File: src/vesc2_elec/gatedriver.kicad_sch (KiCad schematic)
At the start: 1 part, among them U101 DRV8301

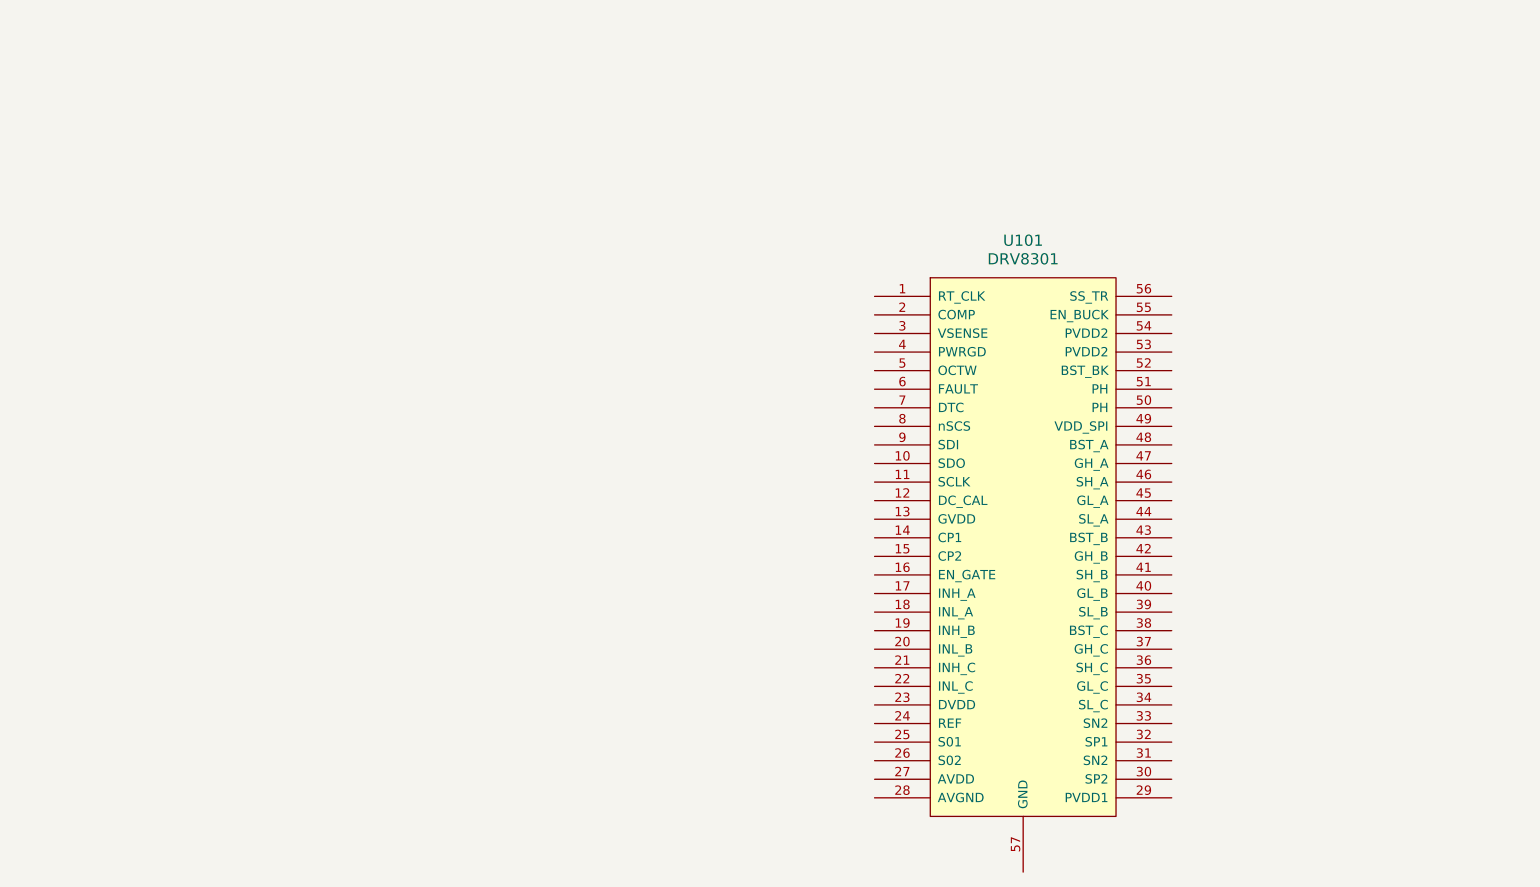
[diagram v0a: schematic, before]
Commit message: recreate gate driver looking less ugly
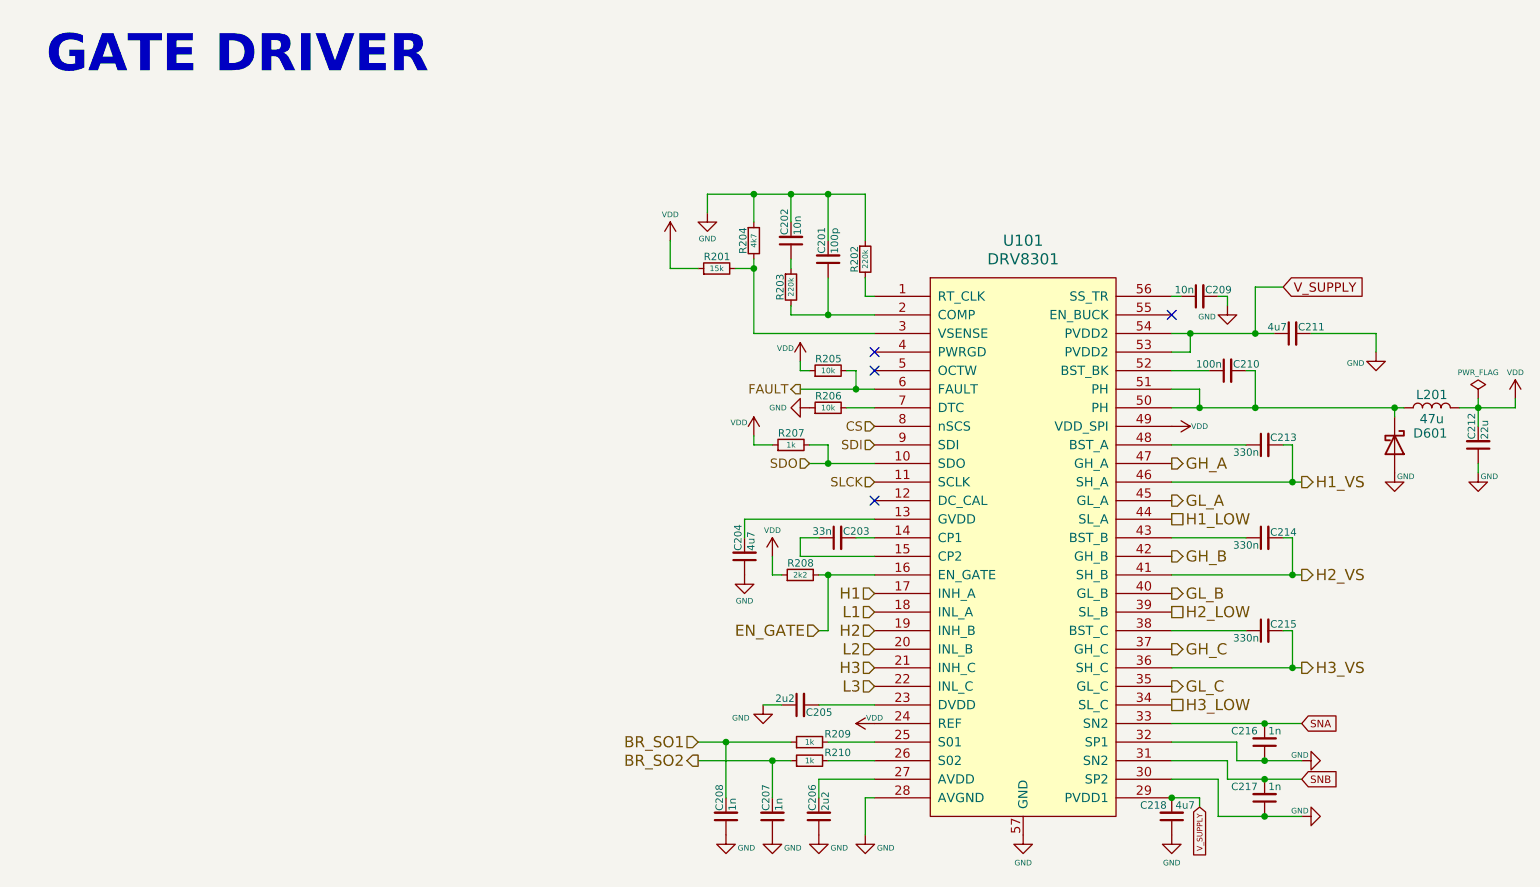
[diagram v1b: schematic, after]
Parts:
- added C201: 100p, Capacitor_SMD:C_0402_1005Metric, symbol Bluesat:C_CompactV
- added C202: 10n, Capacitor_SMD:C_0402_1005Metric, symbol Bluesat:C_CompactV
- added C203: 33n, Capacitor_SMD:C_0603_1608Metric, symbol Bluesat:C_CompactH
- added C204: 4u7, Capacitor_SMD:C_1206_3216Metric, symbol Bluesat:C_CompactV
- added C205: 2u2, Capacitor_SMD:C_0603_1608Metric, symbol Bluesat:C_CompactH
- added C206: 2u2, Capacitor_SMD:C_0603_1608Metric, symbol Bluesat:C_CompactV
- added C207, C208, C216, C217: 1n, Capacitor_SMD:C_0402_1005Metric, symbol Bluesat:C_CompactV
- added C209: 10n, Capacitor_SMD:C_0402_1005Metric, symbol Bluesat:C_CompactH
- added C210: 100n, Capacitor_SMD:C_0603_1608Metric, symbol Bluesat:C_CompactH
- added C211: 4u7, Capacitor_SMD:C_1210_3225Metric, symbol Bluesat:C_CompactH
- added C212: 22u, Capacitor_SMD:C_1210_3225Metric, symbol Bluesat:C_CompactV
- added C213, C214, C215: 330n, Capacitor_SMD:C_0603_1608Metric, symbol Bluesat:C_CompactH
- added C218: 4u7, Capacitor_SMD:C_1210_3225Metric, symbol Bluesat:C_CompactV
- added D601: D_Schottky, Diode_SMD:D_SOD-123, symbol Device:D_Schottky
- added L201: 47u, Inductor_SMD:L_Changjiang_FXL0630, symbol Device:L
- added R201: 15k, Resistor_SMD:R_0402_1005Metric, symbol Bluesat:R_CompactH
- added R202, R203: 220k, Resistor_SMD:R_0402_1005Metric, symbol Bluesat:R_CompactV
- added R204: 4k7, Resistor_SMD:R_0402_1005Metric, symbol Bluesat:R_CompactV
- added R205, R206: 10k, Resistor_SMD:R_0402_1005Metric, symbol Bluesat:R_CompactH
- added R207, R209, R210: 1k, Resistor_SMD:R_0402_1005Metric, symbol Bluesat:R_CompactH
- added R208: 2k2, Resistor_SMD:R_0402_1005Metric, symbol Bluesat:R_CompactH
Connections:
- net at U101.1 (RT_CLK): now also R202.2
- net SDO: now reaches U101.10 (SDO)
- net SDO: now also R207.2
- net SLCK: now reaches U101.11 (SCLK)
- net at U101.13 (GVDD): now also C204.2
- net at U101.14 (CP1): now also C203.2
- net at U101.15 (CP2): now also C203.1
- net EN_GATE: now reaches U101.16 (EN_GATE)
- net EN_GATE: now also R208.2
- net H1: now reaches U101.17 (INH_A)
- net L1: now reaches U101.18 (INL_A)
- net H2: now reaches U101.19 (INH_B)
- net at U101.2 (COMP): now also C201.1, R203.2
- net L2: now reaches U101.20 (INL_B)
- net H3: now reaches U101.21 (INH_C)
- net L3: now reaches U101.22 (INL_C)
- net at U101.23 (DVDD): now also C205.2
- net VDD: now reaches U101.24 (REF)
- net VDD: now also U101.49 (VDD_SPI), C212.2, L201.2, R201.1, R205.1, R207.1, R208.1
- net at U101.25 (S01): now also R209.2
- net at U101.26 (S02): now also R210.2
- net at U101.27 (AVDD): now also C206.2
- net GND: now reaches U101.28 (AVGND)
- net GND: now also U101.30 (SP2), U101.32 (SP1), U101.57 (GND), C201.2, C202.2, C204.1, C205.1, C206.1, C207.1, C208.1, C209.2, C211.2, C212.1, C216.1, C217.1, C218.1, D601.2 (A), R202.1, R204.1, R206.1
- net V_SUPPLY: now reaches U101.29 (PVDD1)
- net V_SUPPLY: now also U101.53 (PVDD2), U101.54 (PVDD2), C211.1, C218.2
- net at U101.3 (VSENSE): now also R201.2, R204.2
- net SNB: now reaches U101.31 (SN2)
- net SNB: now also C217.2
- net SNA: now reaches U101.33 (SN2)
- net SNA: now also C216.2
- net H3_LOW: now reaches U101.34 (SL_C)
- net GL_C: now reaches U101.35 (GL_C)
- net H3_VS: now reaches U101.36 (SH_C)
- net H3_VS: now also C215.2
- net GH_C: now reaches U101.37 (GH_C)
- net at U101.38 (BST_C): now also C215.1
- net H2_LOW: now reaches U101.39 (SL_B)
- net GL_B: now reaches U101.40 (GL_B)
- net H2_VS: now reaches U101.41 (SH_B)
- net H2_VS: now also C214.2
- net GH_B: now reaches U101.42 (GH_B)
- net at U101.43 (BST_B): now also C214.1
- net H1_LOW: now reaches U101.44 (SL_A)
- net GL_A: now reaches U101.45 (GL_A)
- net H1_VS: now reaches U101.46 (SH_A)
- net H1_VS: now also C213.2
- net GH_A: now reaches U101.47 (GH_A)
- net at U101.48 (BST_A): now also C213.1
- net at U101.50 (PH): now also U101.51 (PH), C210.2, D601.1 (K), L201.1
- net at U101.52 (BST_BK): now also C210.1
- net at U101.56 (SS_TR): now also C209.1
- net FAULT: now reaches U101.6 (FAULT)
- net FAULT: now also R205.2
- net at U101.7 (DTC): now also R206.2
- net CS: now reaches U101.8 (nSCS)
- net SDI: now reaches U101.9 (SDI)
- new net: C202.1, R203.1
- new net BR_SO1: C208.2, R209.1
- new net BR_SO2: C207.2, R210.1
- no-connect marks 0 -> 4
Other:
- note added: "GATE DRIVER"
- moved on the sheet: U101

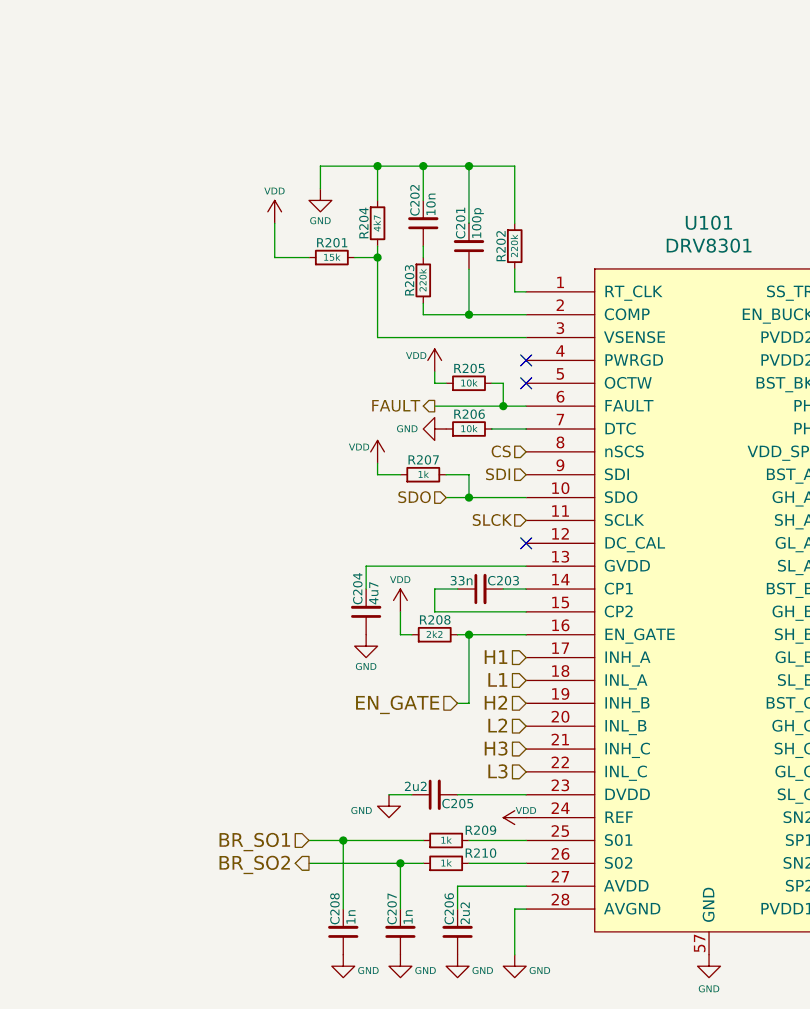
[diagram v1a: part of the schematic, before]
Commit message: configure STM32G4 and route
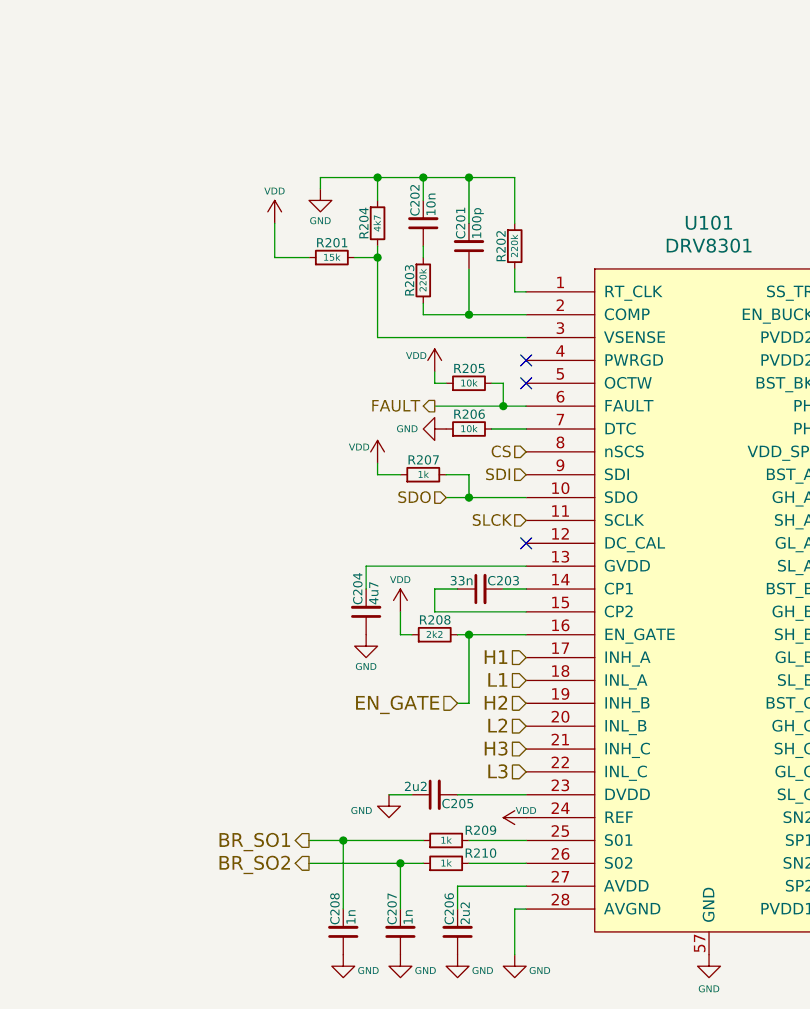
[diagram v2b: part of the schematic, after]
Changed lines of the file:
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@@
+	)
+	(junction
+		(at 114.3 39.37)
+		(diameter 0)
+		(color 0 0 0 0)
+	)
+	(junction
+		(at 109.22 39.37)
+		(diameter 0)
+		(color 0 0 0 0)
 	)
 	(junction
@@
 	)
 	(junction
-		(at 114.3 38.1)
-		(diameter 0)
-		(color 0 0 0 0)
-	)
-	(junction
 		(at 208.28 67.31)
 		(diameter 0)
@@
 	)
 	(junction
-		(at 119.38 38.1)
-		(diameter 0)
-		(color 0 0 0 0)
-	)
-	(junction
 		(at 170.18 67.31)
 		(diameter 0)
@@
 	)
 	(junction
-		(at 109.22 38.1)
-		(diameter 0)
-		(color 0 0 0 0)
-	)
-	(junction
 		(at 182.88 77.47)
+		(diameter 0)
+		(color 0 0 0 0)
+	)
+	(junction
+		(at 119.38 39.37)
 		(diameter 0)
 		(color 0 0 0 0)
@@
 	(wire
 		(pts
-			(xy 102.87 38.1) (xy 102.87 40.64)
+			(xy 102.87 39.37) (xy 102.87 40.64)
 		)
 		(stroke
@@
 	(wire
 		(pts
-			(xy 124.46 38.1) (xy 124.46 44.45)
+			(xy 124.46 39.37) (xy 124.46 44.45)
 		)
 		(stroke
@@
 	(wire
 		(pts
-			(xy 114.3 41.91) (xy 114.3 38.1)
+			(xy 114.3 41.91) (xy 114.3 39.37)
 		)
 		(stroke
@@
 	(wire
 		(pts
-			(xy 119.38 38.1) (xy 114.3 38.1)
-		)
-		(stroke
-			(width 0)
-			(type default)
-		)
-	)
-	(wire
-		(pts
-			(xy 124.46 38.1) (xy 119.38 38.1)
+			(xy 119.38 39.37) (xy 114.3 39.37)
+		)
+		(stroke
+			(width 0)
+			(type default)
+		)
+	)
+	(wire
+		(pts
+			(xy 124.46 39.37) (xy 119.38 39.37)
 		)
 		(stroke
@@
 	(wire
 		(pts
-			(xy 109.22 38.1) (xy 102.87 38.1)
+			(xy 109.22 39.37) (xy 102.87 39.37)
 		)
 		(stroke
@@
 	(wire
 		(pts
-			(xy 109.22 38.1) (xy 114.3 38.1)
+			(xy 109.22 39.37) (xy 114.3 39.37)
 		)
 		(stroke
@@
 	(wire
 		(pts
-			(xy 109.22 41.91) (xy 109.22 38.1)
+			(xy 109.22 41.91) (xy 109.22 39.37)
 		)
 		(stroke
@@
 	(wire
 		(pts
-			(xy 119.38 44.45) (xy 119.38 38.1)
+			(xy 119.38 44.45) (xy 119.38 39.37)
 		)
 		(stroke
@@
 	)
 	(hierarchical_label "BR_SO1"
-		(shape input)
+		(shape output)
 		(at 101.6 113.03 180)
 		(effects

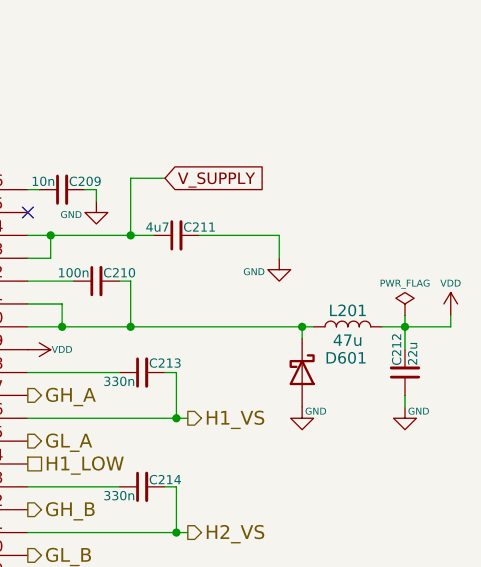
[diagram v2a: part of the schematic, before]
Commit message: Finish schem bar mosfet footprints
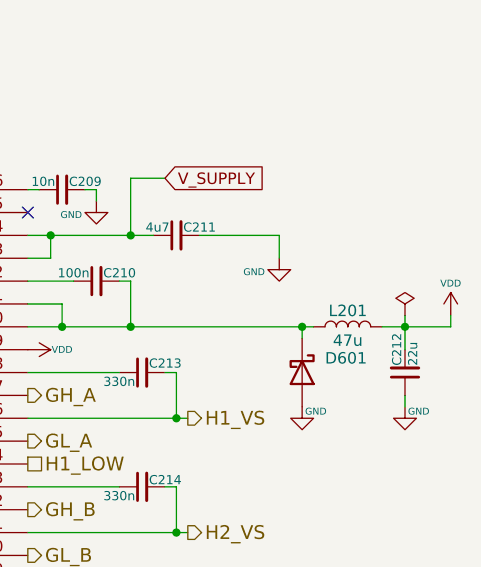
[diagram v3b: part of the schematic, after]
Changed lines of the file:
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@@
 					(size 0.762 0.762)
 				)
+				(hide yes)
 			)
 		)

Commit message: Final commit before routing just incase
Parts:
- renumbered C208 to C201, C204 to C202, C207 to C203, C202 to C204, C201 to C207, C203 to C208, C218 to C209, C209 to C210, C210 to C211, C213 to C212, C214 to C213, C215 to C214, C216 to C215, C217 to C216, C211 to C217, C212 to C218, D601 to D201, R204 to R202, R207 to R204, R208 to R205, R209 to R206, R210 to R207, R205 to R208, R206 to R209, R202 to R210, U101 to U201

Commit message: finished routing :)
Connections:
- net V_SUPPLY: no longer C217.1, U201.53 (PVDD2), U201.54 (PVDD2)
- new net VBUS: C217.1, U201.53 (PVDD2), U201.54 (PVDD2)
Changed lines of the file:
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@@
-	(wire
-		(pts
-			(xy 177.8 50.8) (xy 181.61 50.8)
-		)
-		(stroke
-			(width 0)
-			(type default)
-		)
-	)
 	(wire
 		(pts
@@
 	(wire
 		(pts
-			(xy 177.8 57.15) (xy 177.8 50.8)
+			(xy 177.8 57.15) (xy 177.8 52.07)
 		)
 		(stroke
@@
 		(property "Intersheetrefs" "${INTERSHEET_REFS}"
 			(at 189.2823 110.49 0)
-			(effects
-				(font
-					(size 1.27 1.27)
-				)
-				(justify left)
-				(hide yes)
-			)
-		)
-	)
-	(global_label "V_SUPPLY"
-		(shape input)
-		(at 181.61 50.8 0)
-		(fields_autoplaced yes)
-		(effects
-			(font
-				(size 1.27 1.27)
-			)
-			(justify left)
-		)
-		(property "Intersheetrefs" "${INTERSHEET_REFS}"
-			(at 193.8481 50.8 0)
 			(effects
 				(font
@@
 					(unit 1)
 				)
+			)
+		)
+	)
+	(symbol
+		(lib_id "power:VBUS")
+		(at 177.8 52.07 0)
+		(unit 1)
+		(exclude_from_sim no)
+		(in_bom yes)
+		(on_board yes)
+		(dnp no)
+		(property "Reference" "#PWR0224"
+			(at 177.8 55.88 0)
+			(effects
+				(font
+					(size 1.27 1.27)
+				)
+				(hide yes)
+			)
+		)
+		(property "Value" "VBUS"
+			(at 177.8 48.26 0)
+			(effects
+				(font
+					(size 1.27 1.27)
+				)
+			)
+		)
+		(property "Footprint" ""
+			(at 177.8 52.07 0)
+			(effects
+				(font
+					(size 1.27 1.27)
+				)
+				(hide yes)
+			)
+		)
+		(property "Datasheet" ""
+			(at 177.8 52.07 0)
+			(effects
+				(font
+					(size 1.27 1.27)
+				)
+				(hide yes)
+			)
+		)
+		(property "Description" "Power symbol creates a global label with name \"VBUS\""
+			(at 177.8 52.07 0)
+			(effects
+				(font
+					(size 1.27 1.27)
+				)
+				(hide yes)
+			)
+		)
+		(pin "1"
+		)
+		(instances
+			(project "vesc2"
+				(path "/2059a583-03d9-42e7-b042-844898d8f177/338ab53d-4fa6-4b23-a24e-1380829c260b"
+					(reference "#PWR0224")
+					(unit 1)
+				)

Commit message: Fix small global label error
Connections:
- net V_SUPPLY is gone; now on net VBUS: C209.2, U201.29 (PVDD1)
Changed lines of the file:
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@@
 	(wire
 		(pts
-			(xy 170.18 120.65) (xy 170.18 121.92)
-		)
-		(stroke
-			(width 0)
-			(type default)
-		)
-	)
-	(wire
-		(pts
 			(xy 182.88 72.39) (xy 182.88 77.47)
 		)
@@
 	(wire
 		(pts
-			(xy 166.37 120.65) (xy 170.18 120.65)
+			(xy 166.37 120.65) (xy 168.91 120.65)
 		)
 		(stroke
@@
 		)
 	)
-	(global_label "V_SUPPLY"
-		(shape input)
-		(at 170.18 121.92 270)
-		(fields_autoplaced yes)
-		(effects
-			(font
-				(size 0.762 0.762)
-			)
-			(justify right)
-		)
-		(property "Intersheetrefs" "${INTERSHEET_REFS}"
-			(at 170.18 129.2631 90)
-			(effects
-				(font
-					(size 1.27 1.27)
-				)
-				(justify right)
-				(hide yes)
-			)
-		)
-	)
 	(global_label "SNB"
 		(shape input)
@@
 					(unit 1)
 				)
+			)
+		)
+	)
+	(symbol
+		(lib_id "power:VBUS")
+		(at 168.91 120.65 270)
+		(unit 1)
+		(exclude_from_sim no)
+		(in_bom yes)
+		(on_board yes)
+		(dnp no)
+		(property "Reference" "#PWR01"
+			(at 165.1 120.65 0)
+			(effects
+				(font
+					(size 1.27 1.27)
+				)
+				(hide yes)
+			)
+		)
+		(property "Value" "VBUS"
+			(at 167.386 119.38 90)
+			(effects
+				(font
+					(size 1.27 1.27)
+				)
+			)
+		)
+		(property "Footprint" ""
+			(at 168.91 120.65 0)
+			(effects
+				(font
+					(size 1.27 1.27)
+				)
+				(hide yes)
+			)
+		)
+		(property "Datasheet" ""
+			(at 168.91 120.65 0)
+			(effects
+				(font
+					(size 1.27 1.27)
+				)
+				(hide yes)
+			)
+		)
+		(property "Description" "Power symbol creates a global label with name \"VBUS\""
+			(at 168.91 120.65 0)
+			(effects
+				(font
+					(size 1.27 1.27)
+				)
+				(hide yes)
+			)
+		)
+		(pin "1"
+		)
+		(instances
+			(project "vesc2"
+				(path "/2059a583-03d9-42e7-b042-844898d8f177/338ab53d-4fa6-4b23-a24e-1380829c260b"
+					(reference "#PWR01")
+					(unit 1)
+				)
